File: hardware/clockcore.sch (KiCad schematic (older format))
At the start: 38 parts, among them J1 Header, J2 USB_C_Receptacle_USB2.0, J3 JTAG Debug Header, Q1 MBT3904DW1T1G, SW1 Reset, SW2 Boot, U1 ESP32-WROOM-32, U2 DS1338Z-33+, U3 FT231XS, U4 USBLC6-4SC6, U5 ‎SN74HCT245PWR‎, Y1 32.768Hz, 12.5pF, 45kΩ

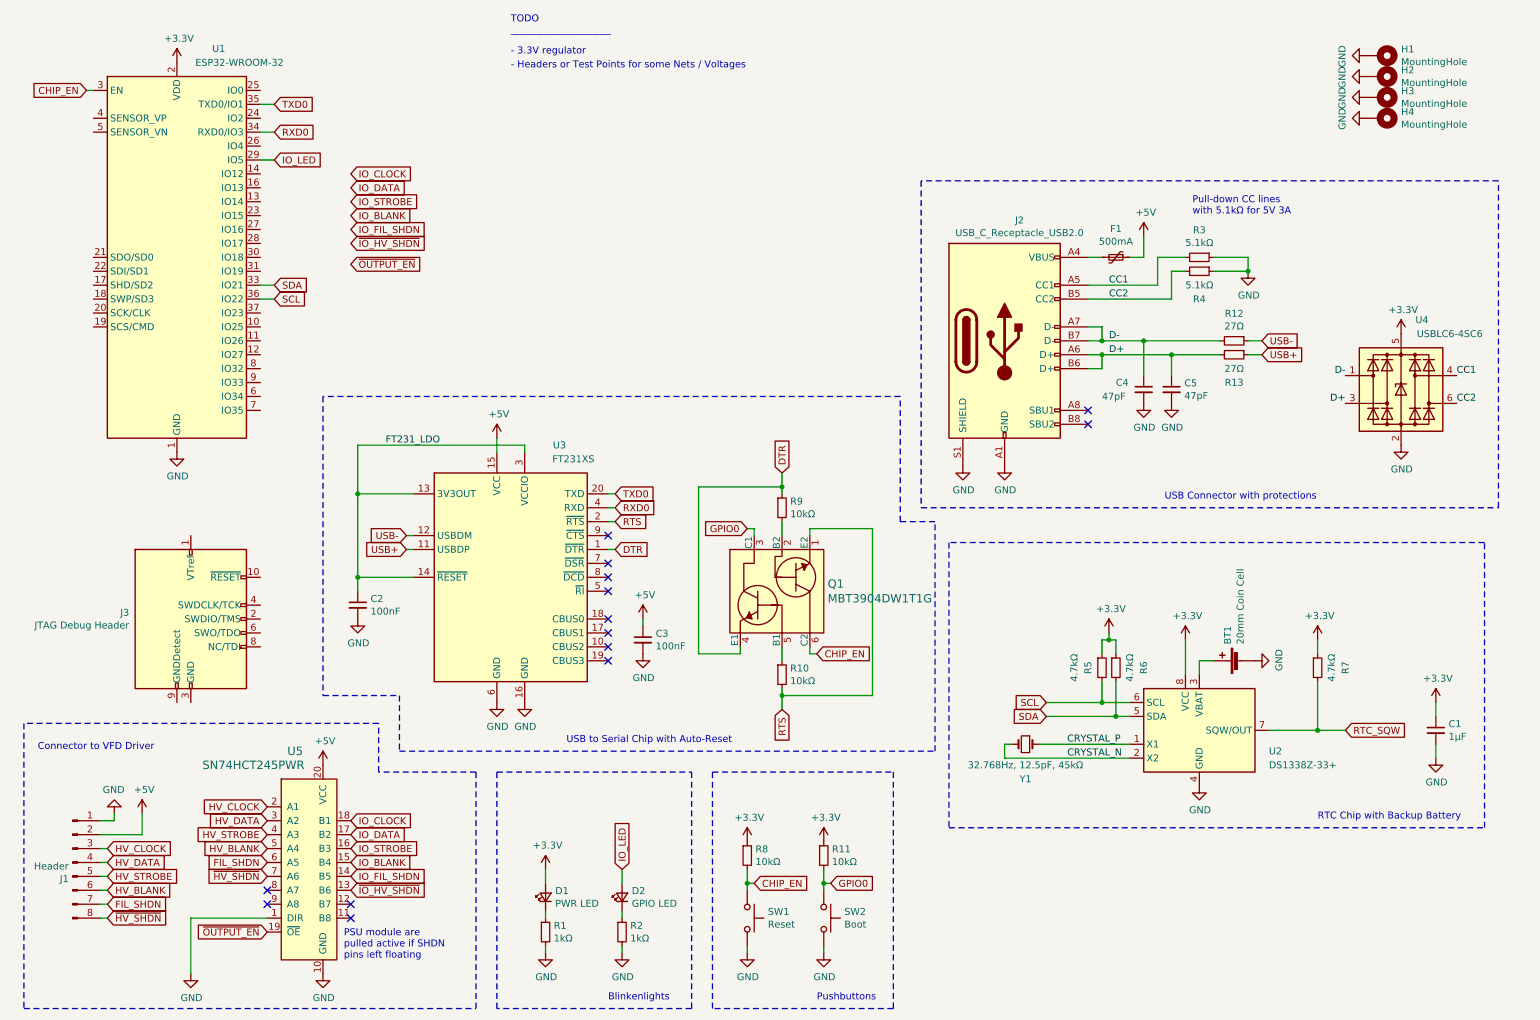
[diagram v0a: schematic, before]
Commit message: finished schematic for clockcore, pcb layout todo
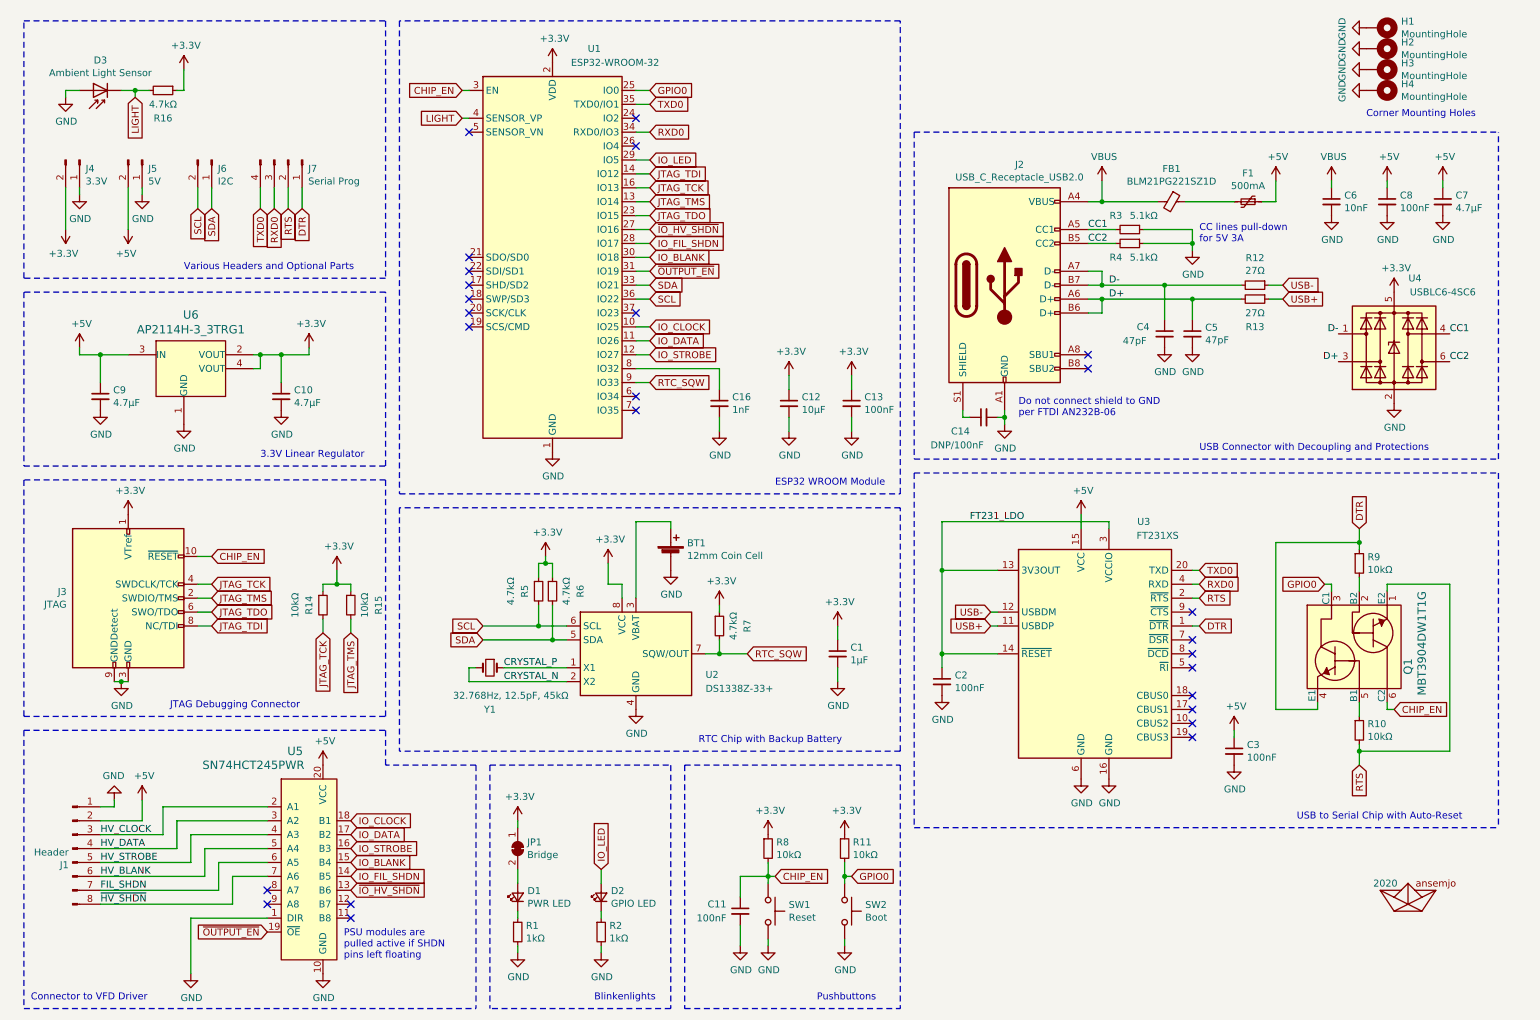
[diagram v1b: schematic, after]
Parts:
- added A1: 2020, extra_libraries:AHOI, symbol ansemjo:ahoi
- added C10, C7, C9: 4.7µF, Capacitor_SMD:C_0805_2012Metric_Pad1.15x1.40mm_HandSolder, symbol Device:C_Small
- added C11, C13, C8: 100nF, Capacitor_SMD:C_0805_2012Metric_Pad1.15x1.40mm_HandSolder, symbol Device:C_Small
- added C12: 10µF, Capacitor_SMD:C_0805_2012Metric_Pad1.15x1.40mm_HandSolder, symbol Device:C_Small
- added C14: DNP/100nF, Capacitor_SMD:C_0805_2012Metric_Pad1.15x1.40mm_HandSolder, symbol Device:C_Small
- added C16: 1nF, Capacitor_SMD:C_0805_2012Metric_Pad1.15x1.40mm_HandSolder, symbol Device:C_Small
- added C6: 10nF, Capacitor_SMD:C_0805_2012Metric_Pad1.15x1.40mm_HandSolder, symbol Device:C_Small
- added D3: Ambient Light Sensor, Diode_SMD:D_1206_3216Metric_Castellated, symbol Device:D_Photo
- added FB1: BLM21PG221SZ1D, Inductor_SMD:L_0805_2012Metric_Pad1.15x1.40mm_HandSolder, symbol Device:Ferrite_Bead_Small
- added J4: 3.3V, Connector_PinHeader_2.54mm:PinHeader_1x02_P2.54mm_Vertical, symbol Connector:Conn_01x02_Male
- added J5: 5V, Connector_PinHeader_2.54mm:PinHeader_1x02_P2.54mm_Vertical, symbol Connector:Conn_01x02_Male
- added J6: I2C, Connector_PinHeader_2.54mm:PinHeader_1x02_P2.54mm_Vertical, symbol Connector:Conn_01x02_Male
- added J7: Serial Prog, Connector_PinHeader_2.54mm:PinHeader_1x04_P2.54mm_Vertical, symbol Connector:Conn_01x04_Male
- added JP1: Bridge, Jumper:SolderJumper-2_P1.3mm_Bridged_RoundedPad1.0x1.5mm, symbol Jumper:SolderJumper_2_Bridged
- added R14, R15: 10kΩ, Resistor_SMD:R_0805_2012Metric_Pad1.15x1.40mm_HandSolder, symbol Device:R_Small
- added R16: 4.7kΩ, Resistor_SMD:R_0805_2012Metric_Pad1.15x1.40mm_HandSolder, symbol Device:R_Small
- added U6: AP2114H-3_3TRG1, digikey-footprints:SOT-223, symbol dk_PMIC-Voltage-Regulators-Linear:AP2114H-3_3TRG1
- BT1: value 20mm Coin Cell -> 12mm Coin Cell; footprint Battery:BatteryHolder_Keystone_3034_1x20mm -> Battery:BatteryHolder_Keystone_3000_1x12mm
- J3: value JTAG Debug Header -> JTAG
- SW1, SW2: footprint Button_Switch_SMD:SW_SPST_B3SL-1002P -> extra_libraries:SW_PTS526_SM08_SMTR2_LFS
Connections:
- net +3V3: now also J3.1 (VTref), C10.1, C12.1, C13.1, J4.2 (Pin_2), JP1.1 (A), R14.1, R15.1, R16.1, U6.2 (VOUT), U6.4 (VOUT); no longer D1.2 (A)
- net +5V: now also C7.1, C8.1, C9.1, J5.2 (Pin_2), U6.3 (IN)
- net CHIP_EN: now also J3.10 (~RESET~), C11.1
- net DTR: now also J7.1 (Pin_1)
- net GND: now also J3.3 (GND), J3.5 (GND), J3.9 (GNDDetect), C10.2, C11.2, C12.2, C13.2, C14.2, C16.2, C6.2, C7.2, C8.2, C9.2, D3.2 (A), J4.1 (Pin_1), J5.1 (Pin_1), U6.1 (GND); no longer J2.S1 (SHIELD)
- net GPIO0: now also U1.25 (IO0)
- net IO_BLANK: now also U1.30 (IO18)
- net IO_CLOCK: now also U1.10 (IO25)
- net IO_DATA: now also U1.11 (IO26)
- net IO_FIL_SHDN: now also U1.28 (IO17)
- net IO_STROBE: now also U1.12 (IO27)
- net RTC_SQW: now also U1.9 (IO33)
- net RTS: now also J7.2 (Pin_2)
- net RXD0: now also J7.3 (Pin_3)
- net SCL: now also J6.2 (Pin_2)
- net SDA: now also J6.1 (Pin_1)
- net TXD0: now also J7.4 (Pin_4)
- net ~IO_HV_SHDN~: now also U1.27 (IO16)
- net ~OUTPUT_EN~: now also U1.31 (IO19)
- net JTAG_TMS: now reaches U1.13 (IO14)
- net JTAG_TMS: now also J3.2 (SWDIO/TMS), R15.2
- net JTAG_TDI: now reaches U1.14 (IO12)
- net JTAG_TDI: now also J3.8 (NC/TDI)
- net JTAG_TCK: now reaches U1.16 (IO13)
- net JTAG_TCK: now also J3.4 (SWDCLK/TCK), R14.2
- net JTAG_TDO: now reaches U1.23 (IO15)
- net JTAG_TDO: now also J3.6 (SWO/TDO)
- net LIGHT: now reaches U1.4 (SENSOR_VP)
- net LIGHT: now also D3.1 (K), R16.2
- net at U1.8 (IO32): now also C16.1
- net VBUS: now reaches J2.A4 (VBUS), J2.A9 (VBUS), J2.B4 (VBUS), J2.B9 (VBUS)
- net VBUS: now also C6.1, FB1.2; no longer F1.2
- new net: F1.2, FB1.1
- new net: C14.1, J2.S1 (SHIELD)
- new net: D1.2 (A), JP1.2 (B)
- no-connect marks 14 -> 26
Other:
- note added: "3.3V Linear Regulator"
- note added: "CC lines pull-down\nfor 5V 3A"
- note added: "Corner Mounting Holes"
- note added: "Do not connect shield to GND\nper FTDI AN232B-06"
- note added: "ESP32 WROOM Module"
- note added: "JTAG Debugging Connector"
- note added: "PSU modules are\npulled active if SHDN\npins left floating"
- note added: "USB Connector with Decoupling and Protections"
- note added: "Various Headers and Optional Parts"
- note removed: "- 3.3V regulator"
- note removed: "- Headers or Test Points for some Nets / Voltages"
- note removed: "PSU module are\npulled active if SHDN\npins left floating"
- note removed: "Pull-down CC lines\nwith 5.1kΩ for 5V 3A"
- note removed: "TODO\n_____________________"
- note removed: "USB Connector with protections"
- moved on the sheet: BT1, C1, C2, C3, C4, C5, D1, D2, F1, H1, H2, H3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

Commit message: finished pcb routing for clockcore, forgot to add zener
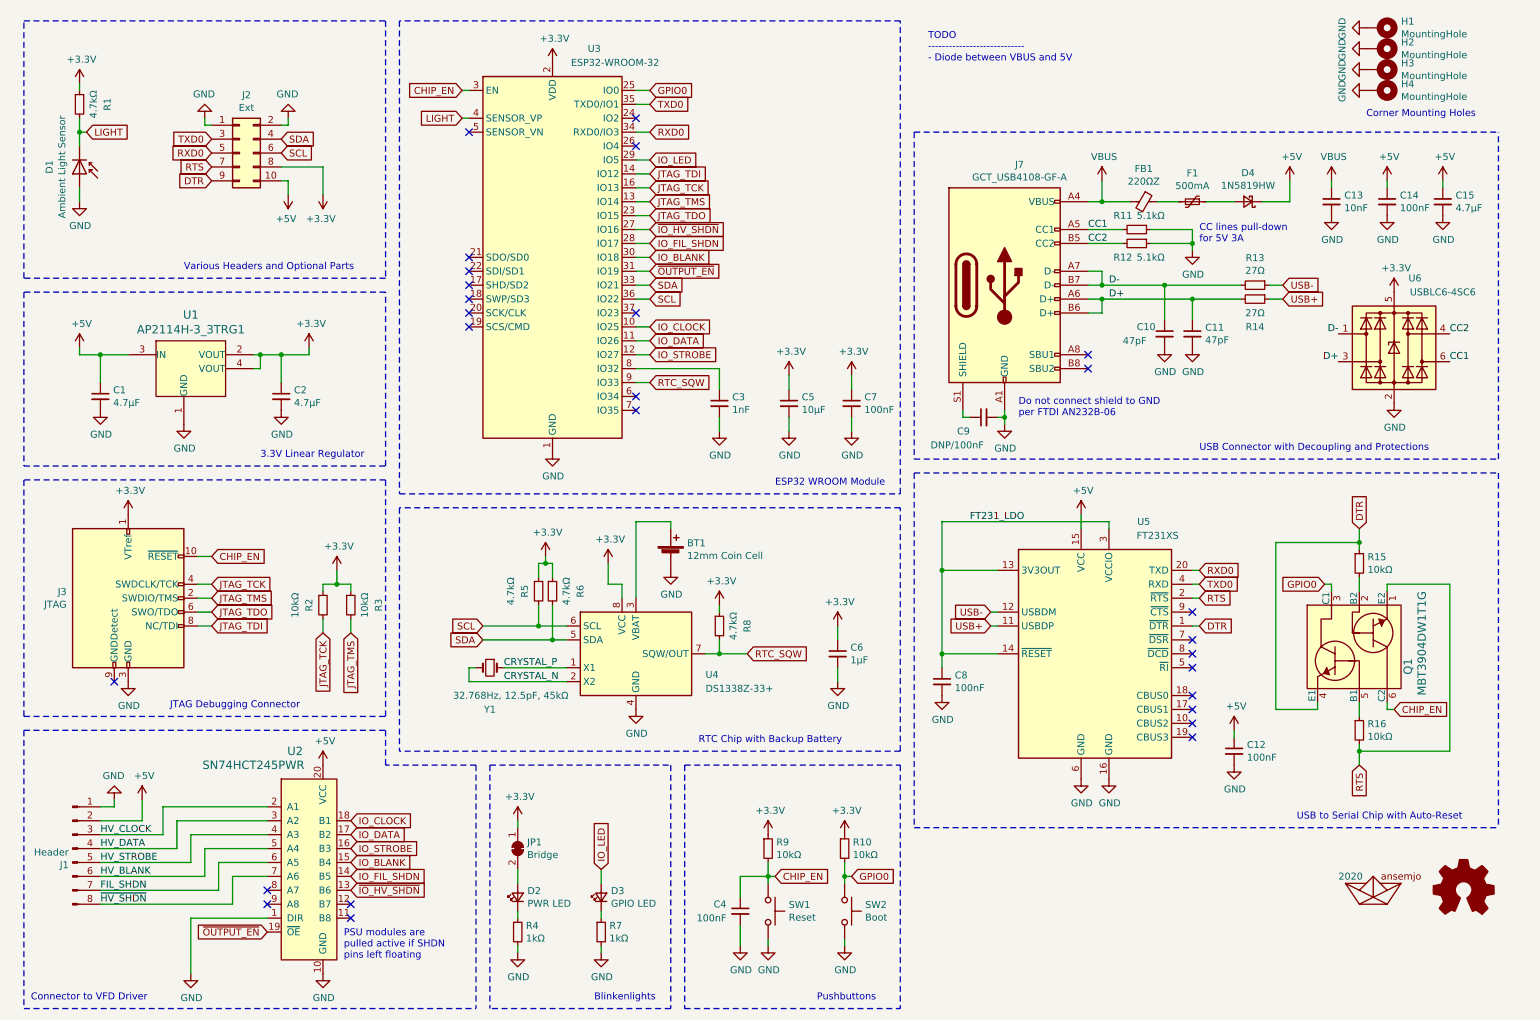
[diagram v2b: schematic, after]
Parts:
- removed J4: 3.3V, Connector_PinHeader_2.54mm:PinHeader_1x02_P2.54mm_Vertical, symbol Connector:Conn_01x02_Male
- removed J5: 5V, Connector_PinHeader_2.54mm:PinHeader_1x02_P2.54mm_Vertical, symbol Connector:Conn_01x02_Male
- removed J6: I2C, Connector_PinHeader_2.54mm:PinHeader_1x02_P2.54mm_Vertical, symbol Connector:Conn_01x02_Male
- removed J7: Serial Prog, Connector_PinHeader_2.54mm:PinHeader_1x04_P2.54mm_Vertical, symbol Connector:Conn_01x04_Male
- added A2: Logo_Open_Hardware_Small, Symbol:OSHW-Logo2_7.3x6mm_SilkScreen, symbol Graphic:Logo_Open_Hardware_Small
- added D4: 1N5819HW, Diode_SMD:D_SOD-123, symbol Device:D_Schottky_Small
- added J2: Ext, Connector_PinHeader_2.54mm:PinHeader_2x05_P2.54mm_Vertical, symbol Connector_Generic:Conn_02x05_Odd_Even
- FB1: value BLM21PG221SZ1D -> 220ΩZ
- J3: footprint Connector_PinHeader_1.27mm:PinHeader_2x05_P1.27mm_Vertical_SMD -> extra_libraries:JTAG_2x05_P1.27mm_Vertical_SMD
- J7: renamed from J2; value USB_C_Receptacle_USB2.0 -> GCT_USB4108-GF-A; footprint Connector_USB:USB_C_Receptacle_GCT_USB4085 -> Connector_USB:USB_C_Receptacle_HRO_TYPE-C-31-M-12
- U1: renamed from U6; footprint digikey-footprints:SOT-223 -> Package_TO_SOT_SMD:SOT-223
- renumbered C9 to C1, C4 to C10, C5 to C11, C3 to C12, C6 to C13, C8 to C14, C7 to C15, C10 to C2, C16 to C3, C11 to C4, C12 to C5, C1 to C6, C13 to C7, C2 to C8, C14 to C9, D3 to D1, D1 to D2, D2 to D3, R16 to R1, R11 to R10, R3 to R11, R4 to R12, R12 to R13, R13 to R14, R9 to R15, R10 to R16, R14 to R2, R15 to R3, R1 to R4, R2 to R7, R7 to R8, R8 to R9, U5 to U2, U1 to U3, U2 to U4, U3 to U5, U4 to U6
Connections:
- net +3V3: now also J2.8 (Pin_8)
- net +5V: now also D4.1 (K), J2.10 (Pin_10); no longer F1.1
- net CC1: now also U6.6 (I/O4); no longer U6.4 (I/O3)
- net CC2: now also U6.4 (I/O3); no longer U6.6 (I/O4)
- net DTR: now also J2.9 (Pin_9)
- net GND: now also J2.1 (Pin_1), J2.2 (Pin_2); no longer J3.9 (GNDDetect)
- net RTS: now also J2.7 (Pin_7)
- net RXD0: now also U5.20 (TXD), J2.5 (Pin_5); no longer U5.4 (RXD)
- net SCL: now also J2.6 (Pin_6)
- net SDA: now also J2.4 (Pin_4)
- net TXD0: now also U5.4 (RXD), J2.3 (Pin_3); no longer U5.20 (TXD)
- new net: D4.2 (A), F1.1
- no-connect marks 26 -> 27
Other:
- note added: "TODO\n----------------------------\n- Diode between VBUS and 5V"
- moved on the sheet: D1, F1, FB1, R1, R11, R12

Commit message: final clockcore design v2_copy ... i think
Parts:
- A2: footprint Symbol:OSHW-Logo2_7.3x6mm_SilkScreen -> Symbol:OSHW-Symbol_6.7x6mm_SilkScreen
- BT1: footprint Battery:BatteryHolder_Keystone_3000_1x12mm -> Battery:BatteryHolder_Keystone_1058_1x2032
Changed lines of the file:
@@
 F 0 "BT1" H 5318 4546 50  0000 L CNN
 F 1 "12mm Coin Cell" H 5318 4455 50  0000 L CNN
-F 2 "Battery:BatteryHolder_Keystone_3000_1x12mm" V 5200 4510 50  0001 C CNN
+F 2 "Battery:BatteryHolder_Keystone_1058_1x2032" V 5200 4510 50  0001 C CNN
 F 3 "https://www.keyelco.com/userAssets/file/M65p9.pdf" V 5200 4510 50  0001 C CNN
 	1    5200 4450
@@
 F 0 "A2" H 10900 7125 50  0001 C CNN
 F 1 "Logo_Open_Hardware_Small" H 10900 6625 50  0001 C CNN
-F 2 "Symbol:OSHW-Logo2_7.3x6mm_SilkScreen" H 10900 7144 50  0001 C CNN
+F 2 "Symbol:OSHW-Symbol_6.7x6mm_SilkScreen" H 10900 7144 50  0001 C CNN
 F 3 "https://github.com/ansemjo/chronovfd" H 10900 6850 50  0001 C CNN
 	1    10900 6850
